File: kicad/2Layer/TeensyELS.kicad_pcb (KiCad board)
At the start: 2 copper layers, 96 x 85 mm, 47 parts, among them J1 RJ45_Shielded, J2 Conn_01x04_Pin, J3 Conn_01x04_Pin, J4 Screw_Terminal_01x02, Q1 BSS138, Q2 BSS138, Q3 BSS138, Q4 BSS138, Q5 BSS138, Q6 BSS138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

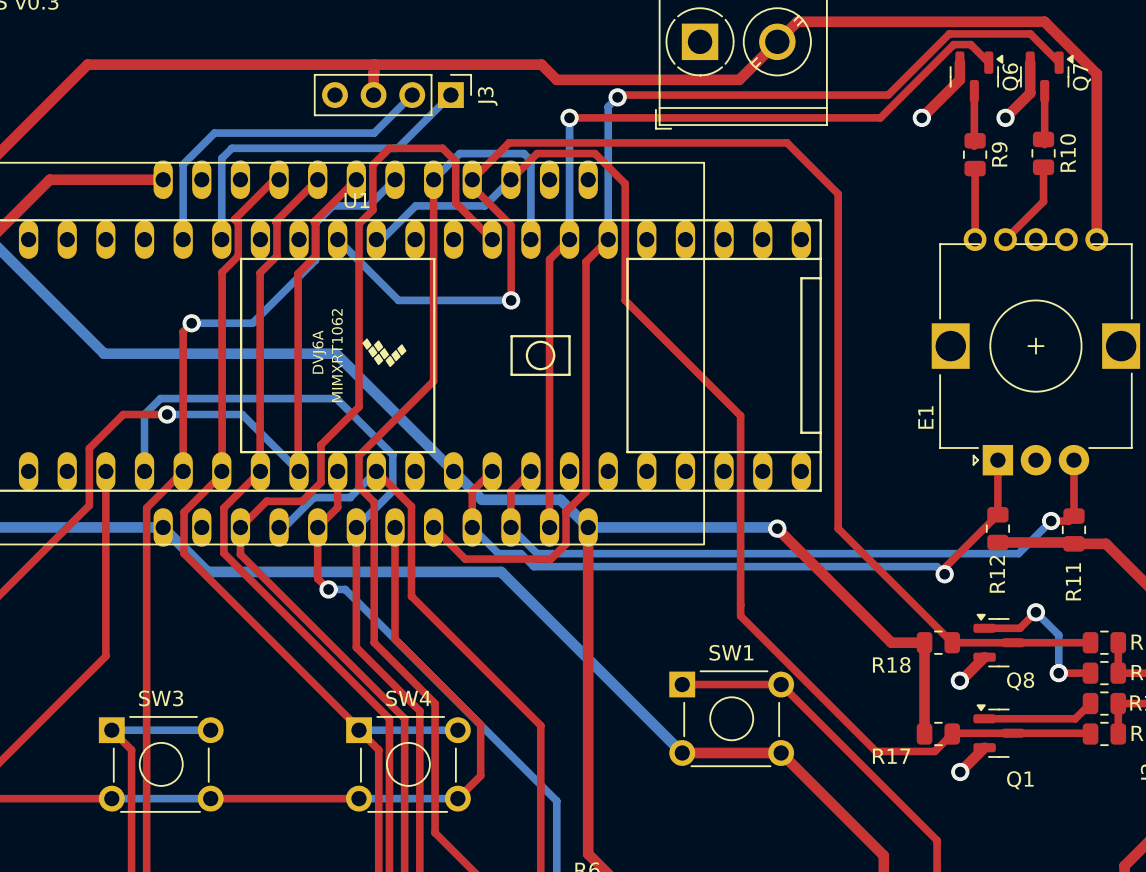
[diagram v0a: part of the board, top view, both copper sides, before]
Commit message: Updated 2 layer designs
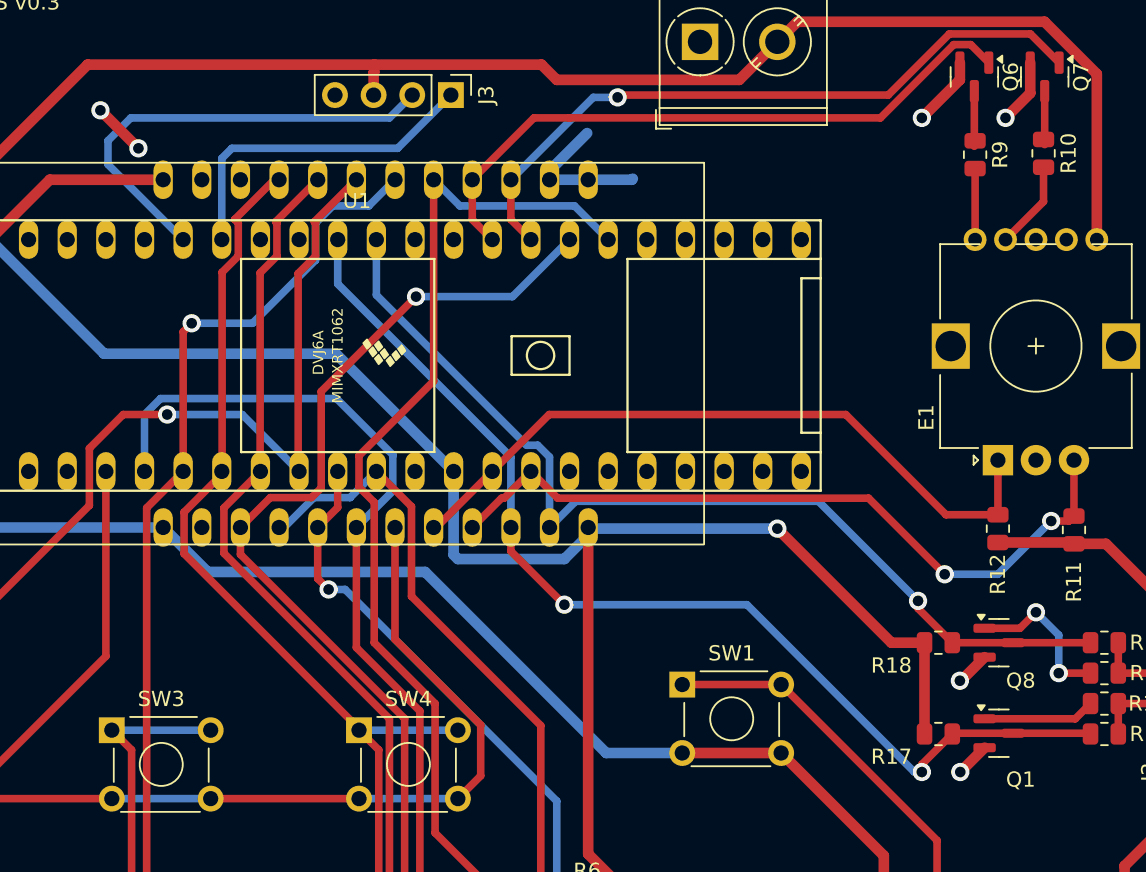
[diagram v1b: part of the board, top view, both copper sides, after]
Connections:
- MCU1 pad 10: /UIEncB -> /EncB
- MCU1 pad 11: /Red -> /EncA
- MCU1 pad 21: /EncA -> /Red
- MCU1 pad 22: /EncB -> /Green
- MCU1 pad 8: /Green -> /UIEncA
- MCU1 pad 9: /UIEncA -> /UIEncB
- U1 pad 30: /Green -> /Ena
- U1 pad 31: /Red -> /Alm
- U1 pad 32: /Ena -> /Green
- U1 pad 33: /Alm -> /Red
- U1 pad 36: /EncB -> /EncA
- U1 pad 37: /EncA -> /EncB
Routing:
- net /Green: track 72.3 -> 45.3 mm
- net /EncA: track 90.2 -> 64.8 mm
- net /Red: track 57.5 -> 42.6 mm, vias 1 -> 0
- net GND: track 21.1 -> 34.2 mm, vias 4 -> 6
- net /SCL: track 21.9 -> 29.8 mm
- net /Alm: track 107.9 -> 100.2 mm, vias 2 -> 3
- net /EncB: track 78.3 -> 70.7 mm, vias 0 -> 2
- net +3.3V: track 248.1 -> 253.3 mm
- net /UIEncB: track 46.7 -> 49.1 mm, vias 1 -> 2
- net /UIEncA: track 45.5 -> 46.5 mm, vias 1 -> 0
- net /Ena: track 94.6 -> 95.2 mm
